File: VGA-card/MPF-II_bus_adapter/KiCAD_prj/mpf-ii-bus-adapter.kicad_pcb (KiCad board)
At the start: 2 copper layers, 98.5 x 35.6 mm, 27 parts, among them J1 Bus_Apple_II_Card_Side, J10 USER1_Sel, J11 INH_Sel, J12 RDY_Sel, J13 COLREF_Sel, J14 IOSTRB_Sel, J15 Q3_Sel, J16 Conn_01x04_Pin, J17 Conn_01x06_Pin, J2 Bus_Apple_II_Computer_Side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

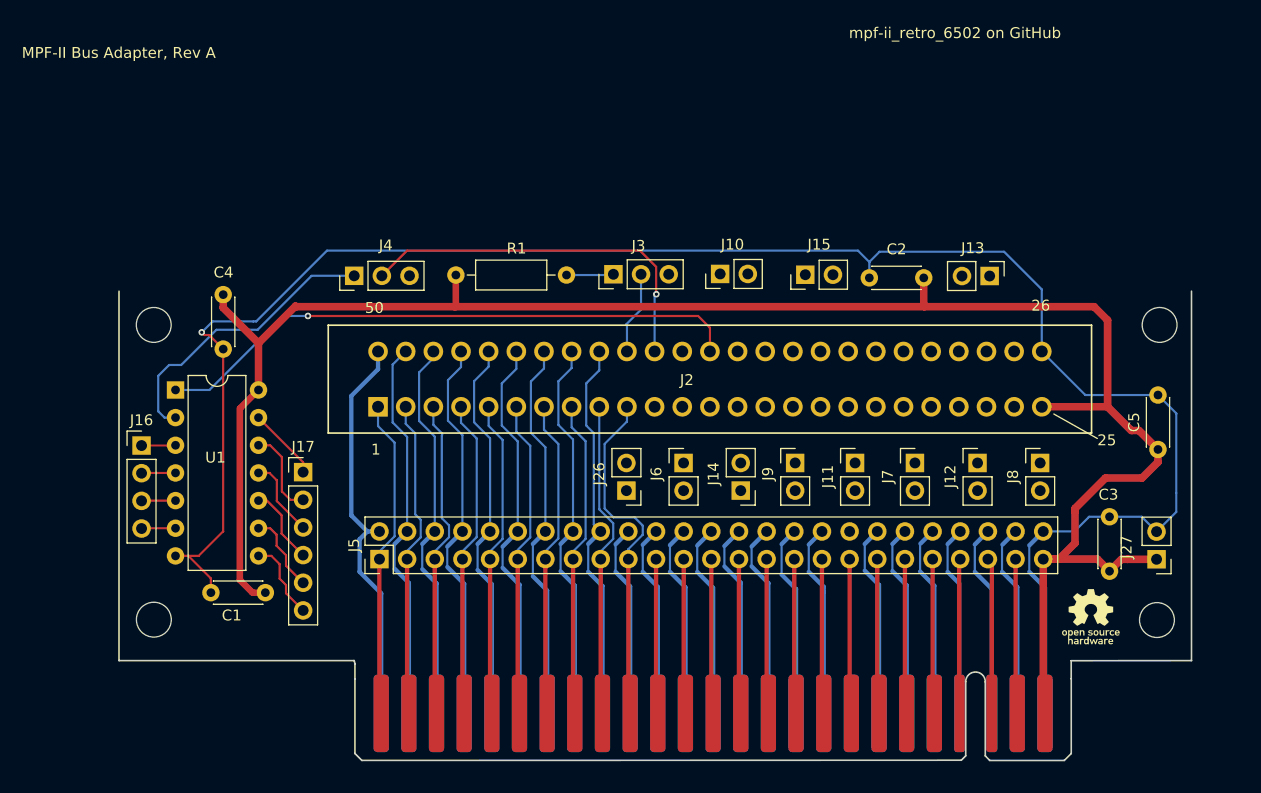
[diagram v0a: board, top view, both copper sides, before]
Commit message: PCB layout finished, ready for testing
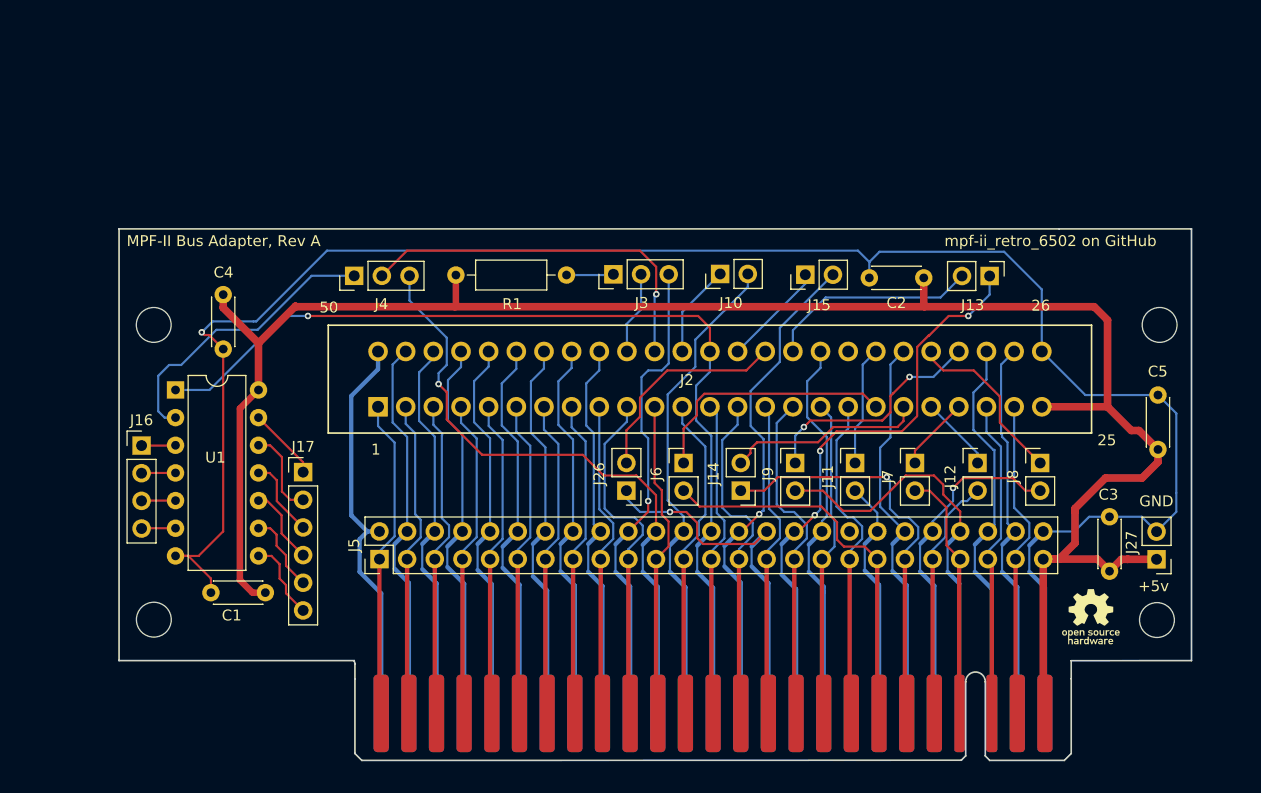
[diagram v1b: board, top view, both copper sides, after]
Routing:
- net /PHI2: track 17.8 -> 58.4 mm, vias 0 -> 1
- net /EXT6: track 17.7 -> 53.5 mm, vias 0 -> 3
- net /2M: track 17.9 -> 46.2 mm, vias 0 -> 1
- net /IODIS: track 17.8 -> 45.3 mm
- net /EXTC: track 17.8 -> 44.1 mm, vias 0 -> 1
- net /EXTE: track 17.0 -> 40.7 mm, vias 0 -> 1
- net /SYNC: track 0.00 -> 23.4 mm
- net /A_NMI: track 0.00 -> 21.6 mm, vias 0 -> 2
- net /EXT8: track 14.2 -> 35.6 mm
- net /M_NMI: track 17.6 -> 38.6 mm
- net /7M: track 0.00 -> 19.8 mm
- net /COLORREF: track 0.00 -> 19.5 mm
- net /RESET: track 17.7 -> 36.1 mm
- net /INTIN: track 17.9 -> 36.0 mm
- net /IOSTRB: track 0.00 -> 18.1 mm
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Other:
- board size 98.5 x 35.6 mm -> 98.5 x 41.3 mm
- board text added: "+5v"
- board text added: "GND"

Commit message: DRC status OK
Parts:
- moved J27 1.21 mm to (190.1, 100.6)
- moved C3 1.14 mm to (185.9, 101.8)
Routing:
- net +5V: track 179.7 -> 175.6 mm
- net /M_DMA: track 19.9 -> 23.9 mm
- net GND: track 175.5 -> 174.6 mm
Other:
- board size 98.5 x 41.3 mm -> 98.1 x 41.3 mm

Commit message: PCB rev. A is ready
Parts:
- moved G*** 1.44 mm to (184.0, 105.8)
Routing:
- net GND: track 174.6 -> 177.8 mm, vias 1 -> 3
- added copper zone on B.Cu, net GND
- added copper zone on F.Cu, net GND
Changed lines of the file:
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@@
 	(title_block
 		(title "Microprofessor-II Bus Adapter Board")
-		(date "2024-07-29")
+		(date "2024-08-01")
 		(rev "A")
 		(comment 1 "Licensed under CERN-OHL-P V2.0 (https://ohwr.org/cern_ohl_p_v2.txt)")
@@
 	(footprint "LOGO"
 		(layer "F.Cu")
-		(at 184.148751 107.234678)
+		(at 184 105.8)
 		(property "Reference" "G***"
 			(at 0 0 0)
@@
 	)
 	(gr_text "mpf-ii_retro_6502 on GitHub"
-		(at 170.7 73.2 0)
+		(at 169.1 73.4 0)
 		(layer "F.SilkS")
 		(effects
@@
 	)
 	(gr_text "MPF-II Bus Adapter, Rev A"
-		(at 95.6 73.2 0)
+		(at 96.3 73.5 0)
 		(layer "F.SilkS")
 		(effects
@@
 	)
 	(segment
+		(start 100.3 82)
+		(end 100.3 82.2)
+		(width 0.2)
+		(layer "F.Cu")
+		(net 2)
+	)
+	(segment
 		(start 103.34 103.61)
 		(end 101.265 101.535)
@@
 	)
 	(segment
+		(start 100.2 81.9)
+		(end 100.3 82)
+		(width 0.2)
+		(layer "F.Cu")
+		(net 2)
+	)
+	(segment
 		(start 102.215 101.535)
 		(end 104.47 99.28)
@@
 		(net 2)
 	)
+	(segment
+		(start 100.3 82.2)
+		(end 102.3 84.2)
+		(width 0.2)
+		(layer "F.Cu")
+		(net 2)
+	)
 	(via
 		(at 102.5 81)
@@
 		(net 2)
 	)
+	(via
+		(at 102.3 84.2)
+		(size 0.6)
+		(drill 0.3)
+		(layers "F.Cu" "B.Cu")
+		(free yes)
+		(net 2)
+	)
+	(via
+		(at 100.2 81.9)
+		(size 0.6)
+		(drill 0.3)
+		(layers "F.Cu" "B.Cu")
+		(free yes)
+		(net 2)
+	)
 	(segment
 		(start 179.78 99.29)
@@
 		(net 77)
 	)
+	(zone
+		(net 2)
+		(net_name "GND")
+		(layer "F.Cu")
+		(hatch edge 0.5)
+		(priority 1)
+		(connect_pads
+			(clearance 0.4)
+		)
+		(min_thickness 0.25)
+		(filled_areas_thickness no)
+		(fill yes
+			(thermal_gap 0.5)
+			(thermal_bridge_width 0.5)
+		)
+		(polygon
+			(pts
+				(xy 94 70.3) (xy 93.9 121.3) (xy 195.1 121.1) (xy 194.7 70.4) (xy 94 70.2)
+			)
+		)
+	)
+	(zone
+		(net 2)
+		(net_name "GND")
+		(layer "B.Cu")
+		(hatch edge 0.5)
+		(connect_pads
+			(clearance 0.4)
+		)
+		(min_thickness 0.25)
+		(filled_areas_thickness no)
+		(fill yes
+			(thermal_gap 0.5)
+			(thermal_bridge_width 0.5)
+		)
+		(polygon
+			(pts
+				(xy 94.4 71.2) (xy 94.4 121) (xy 194.7 120.8) (xy 194.1 70.7) (xy 94.4 70.4)
+			)
+		)
+	)
 )

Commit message: PCB updated, PDF exported
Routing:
- net /M_DMA: track 23.9 -> 23.2 mm
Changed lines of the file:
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@@
-	)
-	(segment
-		(start 171.1 104.52)
-		(end 172.16 103.46)
-		(width 0.2)
-		(layer "F.Cu")
-		(net 23)
 	)
 	(segment
@@
 	)
 	(segment
-		(start 172.16 103.46)
-		(end 172.16 101.83)
+		(start 172.16 101.83)
+		(end 172.16 111.56)
 		(width 0.2)
 		(layer "F.Cu")
@@
 	)
 	(segment
-		(start 171.1 110.7)
-		(end 171.1 104.52)
+		(start 172.16 111.56)
+		(end 172.06 111.66)
 		(width 0.2)
 		(layer "F.Cu")
@@
 		(width 0.2)
 		(layer "F.Cu")
-		(net 23)
-	)
-	(segment
-		(start 172.06 111.66)
-		(end 171.1 110.7)
-		(width 0.2)
-		(layer "F.Cu")

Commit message: PCB updated
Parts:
- moved J26 2.54 mm to (141.4, 93.0), turned to 0 degrees
- moved J14 2.54 mm to (152.0, 93.0), turned to 0 degrees
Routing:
- net /IOSTRB: track 18.1 -> 23.3 mm
- net /7M: track 19.8 -> 24.1 mm, vias 0 -> 1
- net /SOUND_IN: track 34.5 -> 36.8 mm
